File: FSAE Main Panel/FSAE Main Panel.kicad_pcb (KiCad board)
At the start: 2 copper layers, 112 parts, among them J201 USB Micro B, J202 Cortex_Debug, J203 Conn_01x04, J204 TE_84953-6_FPC, Q301 IRLML6402TRPBF, SW1 B3W-1020, SW2 B3W-1020, U1 SAMD21G18A-AU, U301 ZLDO1117-5V, U302 LP2985-3.3, U303 LM1085-5.0, U401 MCP2515-I/ST, U402 MCP2551-I/SN, U501 TLC6C598, U502 TLC6C5816, U503 TLC6C5816, U504 TLC6C5816, Y101 32.768kHz, Y401 Resonator

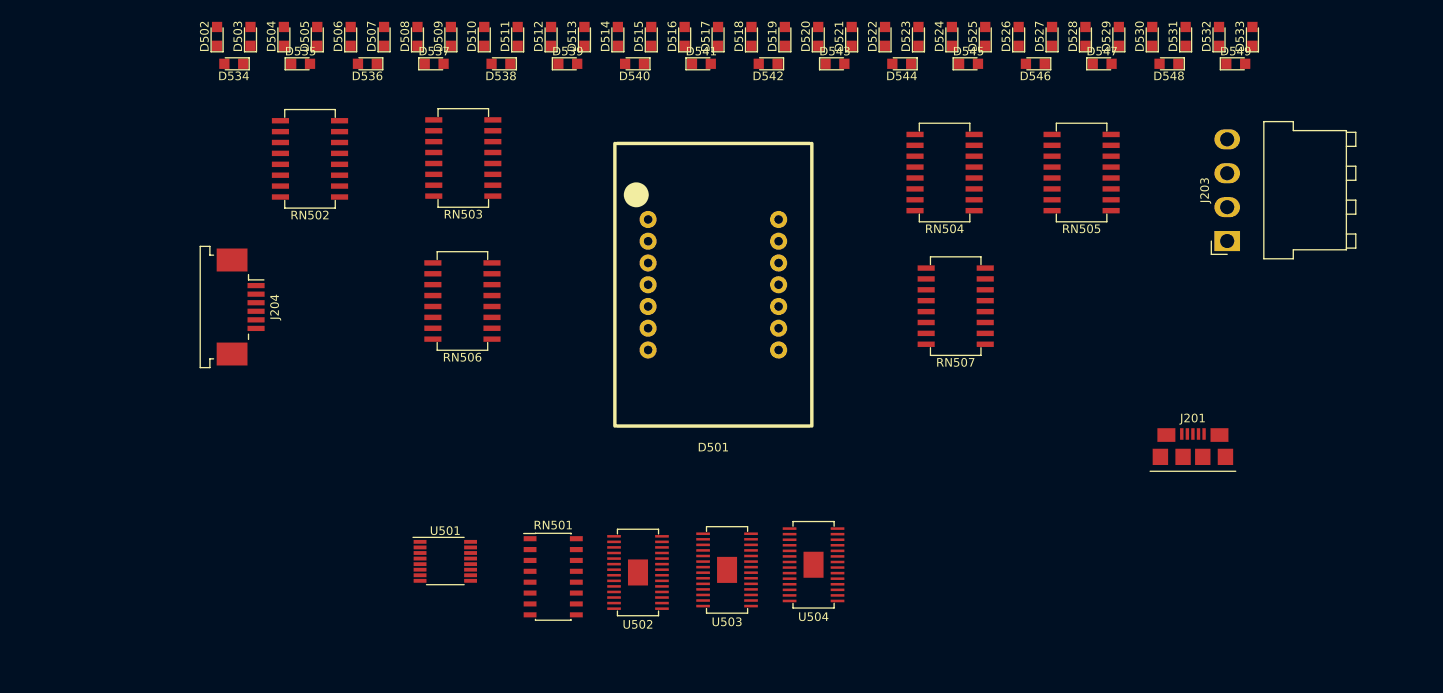
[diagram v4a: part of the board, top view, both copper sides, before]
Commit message: Added Warning Lights
Added Warning lights and started bulk routing
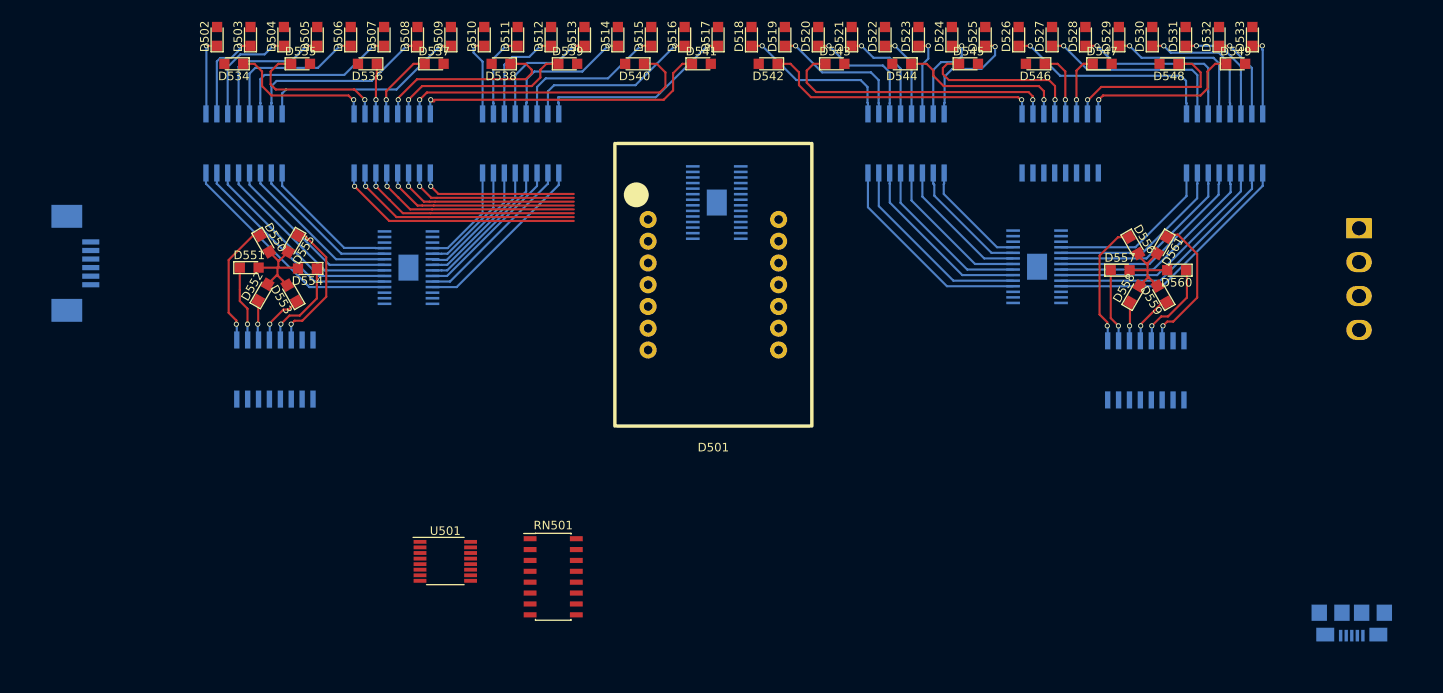
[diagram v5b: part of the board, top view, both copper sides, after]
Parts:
- added D550: LY R976, LEDs:LED_0805, F.Cu at (110.1, 60.7)
- added D551: LY R976, LEDs:LED_0805, F.Cu at (108.3, 63.5)
- added D552: LY R976, LEDs:LED_0805, F.Cu at (109.9, 66.4)
- added D553: LY R976, LEDs:LED_0805, F.Cu at (113.3, 66.5)
- added D554: LY R976, LEDs:LED_0805, F.Cu at (115.1, 63.6)
- added D555: LY R976, LEDs:LED_0805, F.Cu at (113.4, 60.7)
- added D556: LS R976, LEDs:LED_0805, F.Cu at (211.6, 60.9)
- added D557: LS R976, LEDs:LED_0805, F.Cu at (210.0, 63.8)
- added D558: LS R976, LEDs:LED_0805, F.Cu at (211.7, 66.6)
- added D559: LS R976, LEDs:LED_0805, F.Cu at (214.9, 66.6)
- added D560: LS R976, LEDs:LED_0805, F.Cu at (216.6, 63.8)
- added D561: LS R976, LEDs:LED_0805, F.Cu at (214.9, 60.9)
- added RN508: 220 Ohm (8x), Bourns 4800P:Bourns 4800P SOM-16, B.Cu at (111.3, 75.4)
- added RN509: 180 Ohm (8x), Bourns 4800P:Bourns 4800P SOM-16, B.Cu at (213.0, 75.5)
- J201, J203, J204, RN502, RN503, RN504, RN505, RN506, RN507, U502, U503, U504: moved to B.Cu
- moved U503 50.6 mm to (200.3, 63.4)
- moved U502 44.6 mm to (126.9, 63.5)
- moved U504 43.8 mm to (162.9, 55.9)
- moved J201 26.0 mm to (237.1, 103.8)
- moved RN507 22.6 mm to (203.0, 49.0), turned to 90 degrees
- moved RN506 20.1 mm to (125.0, 49.0), turned to 90 degrees
- moved J204 20.0 mm to (88.0, 63.0), turned to 90 degrees
- moved RN505 17.0 mm to (222.2, 49.0), turned to 90 degrees
- moved J203 15.5 mm to (237.9, 58.9), turned to 270 degrees
- moved RN502 7.91 mm to (107.7, 49.0), turned to 90 degrees
- moved RN503 6.91 mm to (140.0, 49.0), turned to 90 degrees
- moved RN504 5.64 mm to (185.0, 49.0), turned to 90 degrees
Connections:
- RN502 pad 1: /Display/RPM_1 -> /Display/RPM_8
- RN502 pad 10: /Display/G7 -> /Display/G2
- RN502 pad 11: /Display/G6 -> /Display/G3
- RN502 pad 12: /Display/G5 -> /Display/G4
- RN502 pad 13: /Display/G4 -> /Display/G5
- RN502 pad 14: /Display/G3 -> /Display/G6
- RN502 pad 15: /Display/G2 -> /Display/G7
- RN502 pad 16: /Display/G1 -> /Display/G8
- RN502 pad 2: /Display/RPM_2 -> /Display/RPM_7
- RN502 pad 3: /Display/RPM_3 -> /Display/RPM_6
- RN502 pad 4: /Display/RPM_4 -> /Display/RPM_5
- RN502 pad 5: /Display/RPM_5 -> /Display/RPM_4
- RN502 pad 6: /Display/RPM_6 -> /Display/RPM_3
- RN502 pad 7: /Display/RPM_7 -> /Display/RPM_2
- RN502 pad 8: /Display/RPM_8 -> /Display/RPM_1
- RN502 pad 9: /Display/G8 -> /Display/G1
- RN503 pad 1: /Display/RPM_9 -> /Display/RPM_16
- RN503 pad 10: /Display/G15 -> /Display/G10
- RN503 pad 11: /Display/G14 -> /Display/G11
- RN503 pad 12: /Display/G13 -> /Display/G12
- RN503 pad 13: /Display/G12 -> /Display/G13
- RN503 pad 14: /Display/G11 -> /Display/G14
- RN503 pad 15: /Display/G10 -> /Display/G15
- RN503 pad 16: /Display/G9 -> /Display/G16
- RN503 pad 2: /Display/RPM_10 -> /Display/RPM_15
- RN503 pad 3: /Display/RPM_11 -> /Display/RPM_14
- RN503 pad 4: /Display/RPM_12 -> /Display/RPM_13
- RN503 pad 5: /Display/RPM_13 -> /Display/RPM_12
- RN503 pad 6: /Display/RPM_14 -> /Display/RPM_11
- RN503 pad 7: /Display/RPM_15 -> /Display/RPM_10
- RN503 pad 8: /Display/RPM_16 -> /Display/RPM_9
- RN503 pad 9: /Display/G16 -> /Display/G9
- RN504 pad 1: /Display/RPM_17 -> /Display/RPM_24
- RN504 pad 10: /Display/Y7 -> /Display/Y2
- RN504 pad 11: /Display/Y6 -> /Display/Y3
- RN504 pad 12: /Display/Y5 -> /Display/Y4
- RN504 pad 13: /Display/Y4 -> /Display/Y5
- RN504 pad 14: /Display/Y3 -> /Display/Y6
- RN504 pad 15: /Display/Y2 -> /Display/Y7
- RN504 pad 16: /Display/Y1 -> /Display/Y8
- RN504 pad 2: /Display/RPM_18 -> /Display/RPM_23
- RN504 pad 3: /Display/RPM_19 -> /Display/RPM_22
- RN504 pad 4: /Display/RPM_20 -> /Display/RPM_21
- RN504 pad 5: /Display/RPM_21 -> /Display/RPM_20
- RN504 pad 6: /Display/RPM_22 -> /Display/RPM_19
- RN504 pad 7: /Display/RPM_23 -> /Display/RPM_18
- RN504 pad 8: /Display/RPM_24 -> /Display/RPM_17
- RN504 pad 9: /Display/Y8 -> /Display/Y1
- RN505 pad 1: /Display/RPM_25 -> /Display/RPM_32
- RN505 pad 10: /Display/R7 -> /Display/R2
- RN505 pad 11: /Display/R6 -> /Display/R3
- RN505 pad 12: /Display/R5 -> /Display/R4
- RN505 pad 13: /Display/R4 -> /Display/R5
- RN505 pad 14: /Display/R3 -> /Display/R6
- RN505 pad 15: /Display/R2 -> /Display/R7
- RN505 pad 16: /Display/R1 -> /Display/R8
- RN505 pad 2: /Display/RPM_26 -> /Display/RPM_31
- RN505 pad 3: /Display/RPM_27 -> /Display/RPM_30
- RN505 pad 4: /Display/RPM_28 -> /Display/RPM_29
- RN505 pad 5: /Display/RPM_29 -> /Display/RPM_28
- RN505 pad 6: /Display/RPM_30 -> /Display/RPM_27
- RN505 pad 7: /Display/RPM_31 -> /Display/RPM_26
- RN505 pad 8: /Display/RPM_32 -> /Display/RPM_25
- RN505 pad 9: /Display/R8 -> /Display/R1
- RN506 pad 1: /Display/SFT_1 -> /Display/SFT_8
- RN506 pad 10: /Display/B7 -> /Display/B2
- RN506 pad 11: /Display/B6 -> /Display/B3
- RN506 pad 12: /Display/B5 -> /Display/B4
- RN506 pad 13: /Display/B4 -> /Display/B5
- RN506 pad 14: /Display/B3 -> /Display/B6
- RN506 pad 15: /Display/B2 -> /Display/B7
- RN506 pad 16: /Display/B1 -> /Display/B8
- RN506 pad 2: /Display/SFT_2 -> /Display/SFT_7
- RN506 pad 3: /Display/SFT_3 -> /Display/SFT_6
- RN506 pad 4: /Display/SFT_4 -> /Display/SFT_5
- RN506 pad 5: /Display/SFT_5 -> /Display/SFT_4
- RN506 pad 6: /Display/SFT_6 -> /Display/SFT_3
- RN506 pad 7: /Display/SFT_7 -> /Display/SFT_2
- RN506 pad 8: /Display/SFT_8 -> /Display/SFT_1
- RN506 pad 9: /Display/B8 -> /Display/B1
- RN507 pad 1: /Display/SFT_9 -> /Display/SFT_16
- RN507 pad 10: /Display/B15 -> /Display/B10
- RN507 pad 11: /Display/B14 -> /Display/B11
- RN507 pad 12: /Display/B13 -> /Display/B12
- RN507 pad 13: /Display/B12 -> /Display/B13
- RN507 pad 14: /Display/B11 -> /Display/B14
- RN507 pad 15: /Display/B10 -> /Display/B15
- RN507 pad 16: /Display/B9 -> /Display/B16
- RN507 pad 2: /Display/SFT_10 -> /Display/SFT_15
- RN507 pad 3: /Display/SFT_11 -> /Display/SFT_14
- RN507 pad 4: /Display/SFT_12 -> /Display/SFT_13
- RN507 pad 5: /Display/SFT_13 -> /Display/SFT_12
- RN507 pad 6: /Display/SFT_14 -> /Display/SFT_11
- RN507 pad 7: /Display/SFT_15 -> /Display/SFT_10
- RN507 pad 8: /Display/SFT_16 -> /Display/SFT_9
- RN507 pad 9: /Display/B16 -> /Display/B9
- Y101 pad 3: GND -> (no net)
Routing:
- net /Display/B7: track 0.00 -> 35.6 mm, vias 0 -> 1
- net /Display/B8: track 0.00 -> 34.9 mm, vias 0 -> 1
- net /Display/B10: track 0.00 -> 33.1 mm, vias 0 -> 1
- net /Display/B9: track 0.00 -> 32.7 mm, vias 0 -> 1
- net /Display/RPM_32: track 0.00 -> 30.7 mm
- net /Display/RPM_31: track 0.00 -> 29.3 mm
- net /Display/SFT_1: track 0.00 -> 28.8 mm, vias 0 -> 1
- net /Display/SFT_2: track 0.00 -> 27.4 mm, vias 0 -> 1
- net /Display/RPM_30: track 0.00 -> 27.2 mm
- net /Display/RPM_1: track 0.00 -> 27.1 mm
- net /Display/SFT_3: track 0.00 -> 26.0 mm, vias 0 -> 1
- net /Display/RPM_29: track 0.00 -> 25.8 mm
- net /Display/RPM_2: track 0.00 -> 25.6 mm
- net /Display/R1: track 0.00 -> 25.1 mm, vias 0 -> 1
- net /Display/RPM_17: track 0.00 -> 24.8 mm
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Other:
- net class Tiny added: clearance 0.175, trace_width 0.175, via_dia 0.4, via_drill 0.3
- net class Wide added: clearance 0.2, trace_width 0.3, via_dia 0.6, via_drill 0.4
- rule trace_min: 0.2 -> 0.175

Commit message: Updated PCB
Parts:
- C101, C102, C103, C104, C105, C106, C107, C108, C201, C202, C203, C204, C301, C302, C303, C304, C305, C306, C501, C502, C503, C504, C505, C506, D201, D301, F201, J202, L101, L201, L301, Q301, R201, R202, R203, R204, R401, R402, R403, RN501, SW1, SW2, U1, U301, U302, U303, U402, U501, Y101, Y401: moved to B.Cu
- U401: footprint Housings_SSOP:TSSOP-20_4.4x6.5mm_Pitch0.65mm -> Housings_SOIC:SOIC-18W_7.5x11.6mm_Pitch1.27mm; moved to B.Cu
- moved SW1 190.4 mm to (89.7, 42.5)
- moved D301 187.1 mm to (229.5, 75.2), turned to 90 degrees
- moved L301 181.7 mm to (234.6, 77.6), turned to 90 degrees
- moved C302 180.8 mm to (229.2, 60.3), turned to 90 degrees
- moved SW2 178.2 mm to (89.7, 52.1)
- moved C301 173.7 mm to (231.0, 80.7), turned to 180 degrees
- moved U301 170.5 mm to (238.8, 84.4)
- moved C303 170.3 mm to (240.6, 78.4), turned to 90 degrees
- moved U303 167.8 mm to (235.0, 66.5)
- moved Q301 150.0 mm to (230.5, 85.8)
- moved C304 140.6 mm to (226.2, 83.5)
- moved C306 137.8 mm to (223.0, 75.4), turned to 270 degrees
- moved L101 134.0 mm to (70.2, 94.8)
- moved C103 133.3 mm to (81.8, 95.6)
- moved C203 132.7 mm to (120.8, 126.4)
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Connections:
- D501 pad 12: Net-(D501-Pad12) -> (no net)
- D501 pad 4: Net-(D501-Pad4) -> (no net)
- D501 pad 5: Net-(D501-Pad5) -> (no net)
- R401 pad 2: Net-(R401-Pad2) -> Net-(U401-Pad2)
- RN508 pad 1: Net-(RN508-Pad1) -> (no net)
- RN508 pad 15: Net-(RN508-Pad15) -> (no net)
- RN508 pad 16: Net-(RN508-Pad16) -> (no net)
- RN508 pad 2: Net-(RN508-Pad2) -> (no net)
- RN509 pad 1: Net-(RN509-Pad1) -> (no net)
- RN509 pad 15: Net-(RN509-Pad15) -> (no net)
- RN509 pad 16: Net-(RN509-Pad16) -> (no net)
- RN509 pad 2: Net-(RN509-Pad2) -> (no net)
- U302 pad 3: Net-(U302-Pad3) -> (no net)
- U302 pad 4: Net-(U302-Pad4) -> (no net)
- U401 pad 10: GND -> (no net)
- U401 pad 11: Net-(U401-Pad11) -> (no net)
- U401 pad 12: Net-(U401-Pad12) -> (no net)
- U401 pad 13: Net-(U401-Pad13) -> CAN_SCLK
- U401 pad 14: CAN_SCLK -> CAN_MOSI
- U401 pad 15: Net-(U401-Pad15) -> CAN_MISO
- U401 pad 16: CAN_MOSI -> CAN_CS
- U401 pad 17: CAN_MISO -> Net-(U401-Pad2)
- U401 pad 18: CAN_CS -> +3V3
- U401 pad 3: Net-(U401-Pad3) -> (no net)
- U401 pad 4: Net-(U401-Pad4) -> (no net)
- U401 pad 5: Net-(U401-Pad5) -> (no net)
- U401 pad 6: Net-(U401-Pad6) -> (no net)
- U401 pad 9: Net-(U401-Pad9) -> GND
- U402 pad 5: Net-(U402-Pad5) -> (no net)
- U501 pad 9: Net-(U501-Pad9) -> (no net)
- U502 pad 26: Net-(U502-Pad26) -> (no net)
- U502 pad 27: Net-(U502-Pad27) -> (no net)
- U503 pad 26: Net-(U503-Pad26) -> (no net)
- U503 pad 27: Net-(U503-Pad27) -> (no net)
- U504 pad 26: Net-(U504-Pad26) -> (no net)
- U504 pad 27: Net-(U504-Pad27) -> (no net)
- Y101 pad 3: (no net) -> GND
- Y401 pad 1: Net-(U401-Pad9) -> Net-(U401-Pad8)
- Y401 pad 3: Net-(U401-Pad8) -> Net-(U401-Pad7)
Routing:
- net Net-(U502-Pad15): track 0.00 -> 107.5 mm, vias 0 -> 4
- net Net-(U503-Pad15): track 0.00 -> 97.3 mm
- net GEAR_IN: track 0.00 -> 90.0 mm, vias 0 -> 4
- net CAN_V+: track 0.00 -> 80.2 mm
- net /Display/a: track 0.00 -> 69.2 mm
- net CAN_H: track 0.00 -> 55.0 mm, vias 0 -> 2
- net /Display/f: track 0.00 -> 54.5 mm
- net /Display/SFT_16: track 0.00 -> 46.5 mm, vias 0 -> 2
- net CAN_L: track 0.00 -> 45.6 mm, vias 0 -> 2
- net /Display/SFT_15: track 0.00 -> 44.8 mm, vias 0 -> 2
- net DWC_+5V: track 0.00 -> 43.8 mm, vias 0 -> 1
- net /Display/SFT_14: track 0.00 -> 43.2 mm, vias 0 -> 2
- net /Display/SFT_13: track 0.00 -> 41.6 mm, vias 0 -> 2
- net /Display/SFT_12: track 0.00 -> 40.0 mm, vias 0 -> 2
- net Net-(U401-Pad2): track 0.00 -> 39.6 mm
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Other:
- board outline added: 160 x 55 mm

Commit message: Updated PCB
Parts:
- moved C501 156.0 mm to (201.7, 71.0), turned to 270 degrees
- moved C502 146.9 mm to (199.4, 71.0), turned to 270 degrees
- moved C505 143.4 mm to (206.5, 67.0)
- moved C506 111.7 mm to (164.2, 62.8), turned to 180 degrees
- moved R202 90.8 mm to (99.8, 42.6), turned to 90 degrees
- moved R201 84.0 mm to (99.8, 47.5), turned to 90 degrees
- moved R204 80.6 mm to (96.8, 51.1), turned to 90 degrees
- moved R203 75.7 mm to (96.8, 55.9), turned to 90 degrees
- moved L101 73.9 mm to (143.3, 84.1)
- moved C504 73.2 mm to (128.2, 69.9), turned to 180 degrees
- moved C201 72.9 mm to (97.4, 47.1), turned to 270 degrees
- moved C202 71.7 mm to (94.5, 55.5), turned to 270 degrees
- moved Y101 70.8 mm to (139.8, 78.0), turned to 180 degrees
- moved C102 66.9 mm to (135.7, 85.6), turned to 270 degrees
- moved J201 66.9 mm to (97.6, 86.8)
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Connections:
- J202 pad 10: Net-(J202-Pad10) -> (no net)
- J202 pad 6: Net-(J202-Pad6) -> (no net)
- J202 pad 7: Net-(J202-Pad7) -> (no net)
- J202 pad 8: Net-(J202-Pad8) -> (no net)
- J202 pad 9: Net-(J202-Pad9) -> (no net)
- U1 pad 11: CAN_CS -> CAN_MOSI
- U1 pad 19: Net-(U1-Pad19) -> GEAR_IN
- U1 pad 25: Net-(U1-Pad25) -> /Display/~G5
- U1 pad 26: Net-(U1-Pad26) -> /Display/~G4
- U1 pad 31: Net-(U1-Pad31) -> /Display/~G3
- U1 pad 32: Net-(U1-Pad32) -> /Display/~G1
- U1 pad 9: CAN_MOSI -> CAN_CS
- U502 pad 3: /Display/~G2 -> /Display/~G1
- U504 pad 15: GEAR_IN -> (no net)
- U504 pad 3: /Display/~G6 -> /Display/~G5
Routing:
- net RPM_SCLK: track 8.41 -> 160.7 mm, vias 1 -> 7
- net RPM_RCLK: track 7.25 -> 152.7 mm, vias 1 -> 4
- net ~RPM_EN: track 6.33 -> 136.9 mm, vias 1 -> 2
- net RPM_CLR: track 7.47 -> 122.8 mm, vias 1 -> 5
- net USB_POWER: track 0.00 -> 112.1 mm
- net ~GEAR_PWM: track 0.00 -> 108.0 mm, vias 0 -> 2
- net GEAR_CLR: track 0.00 -> 106.0 mm, vias 0 -> 4
- net GEAR_RCLK: track 0.00 -> 101.4 mm, vias 0 -> 4
- net GEAR_SCLK: track 0.00 -> 100.1 mm, vias 0 -> 2
- net ~CLEAR: track 0.00 -> 62.7 mm
- net CAN_CS: track 0.00 -> 54.7 mm
- net CAN_MISO: track 0.00 -> 54.3 mm
- net CAN_MOSI: track 0.00 -> 53.5 mm, vias 0 -> 2
- net CAN_SCLK: track 0.00 -> 53.2 mm, vias 0 -> 2
- net ~RESET: track 0.00 -> 48.9 mm, vias 0 -> 4
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- added copper zone on B.Cu, net CAN_V+

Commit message: Updated PCB
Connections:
- U1 pad 48: Net-(U1-Pad48) -> ~CHECK_ENGINE
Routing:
- net /Display/~G3: track 0.00 -> 104.7 mm, vias 0 -> 2
- net /Display/~G4: track 0.00 -> 101.4 mm, vias 0 -> 2
- net /Display/~G5: track 16.5 -> 97.8 mm, vias 0 -> 8
- net ~CHECK_ENGINE: track 0.00 -> 71.3 mm, vias 0 -> 6
- net DWC_SDI: track 0.00 -> 64.4 mm, vias 0 -> 4
- net DWC_SCLK: track 0.00 -> 48.5 mm, vias 0 -> 6
- net DWC_+5V: track 48.1 -> 11.9 mm, vias 1 -> 0
- net (no net): track 9.40 -> 41.8 mm, vias 0 -> 1
- net SWDIO: track 0.00 -> 21.5 mm
- net SWCLK: track 0.00 -> 16.0 mm, vias 0 -> 2
- net /Display/~G1: track 0.65 -> 15.0 mm, vias 0 -> 2
- net +3V3: track 62.0 -> 65.6 mm
- net ~RPM_EN: track 136.9 -> 140.4 mm
- net RPM_CLR: track 122.8 -> 125.6 mm, vias 5 -> 6
- net Net-(U503-Pad15): track 86.4 -> 83.8 mm
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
